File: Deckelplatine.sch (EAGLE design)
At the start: 67 parts, among them IC1 MAX1487EESA+, IC2 74HCT595D, IC3 74HCT595D, IC4 74HCT595D, IC5 74HCT595D, IC6 74HCT595D, J1 52808-2570, Q1 BC846BSMD, Q2 BC846BSMD, U1 LM2676S, X1 236-404, X2 233-502

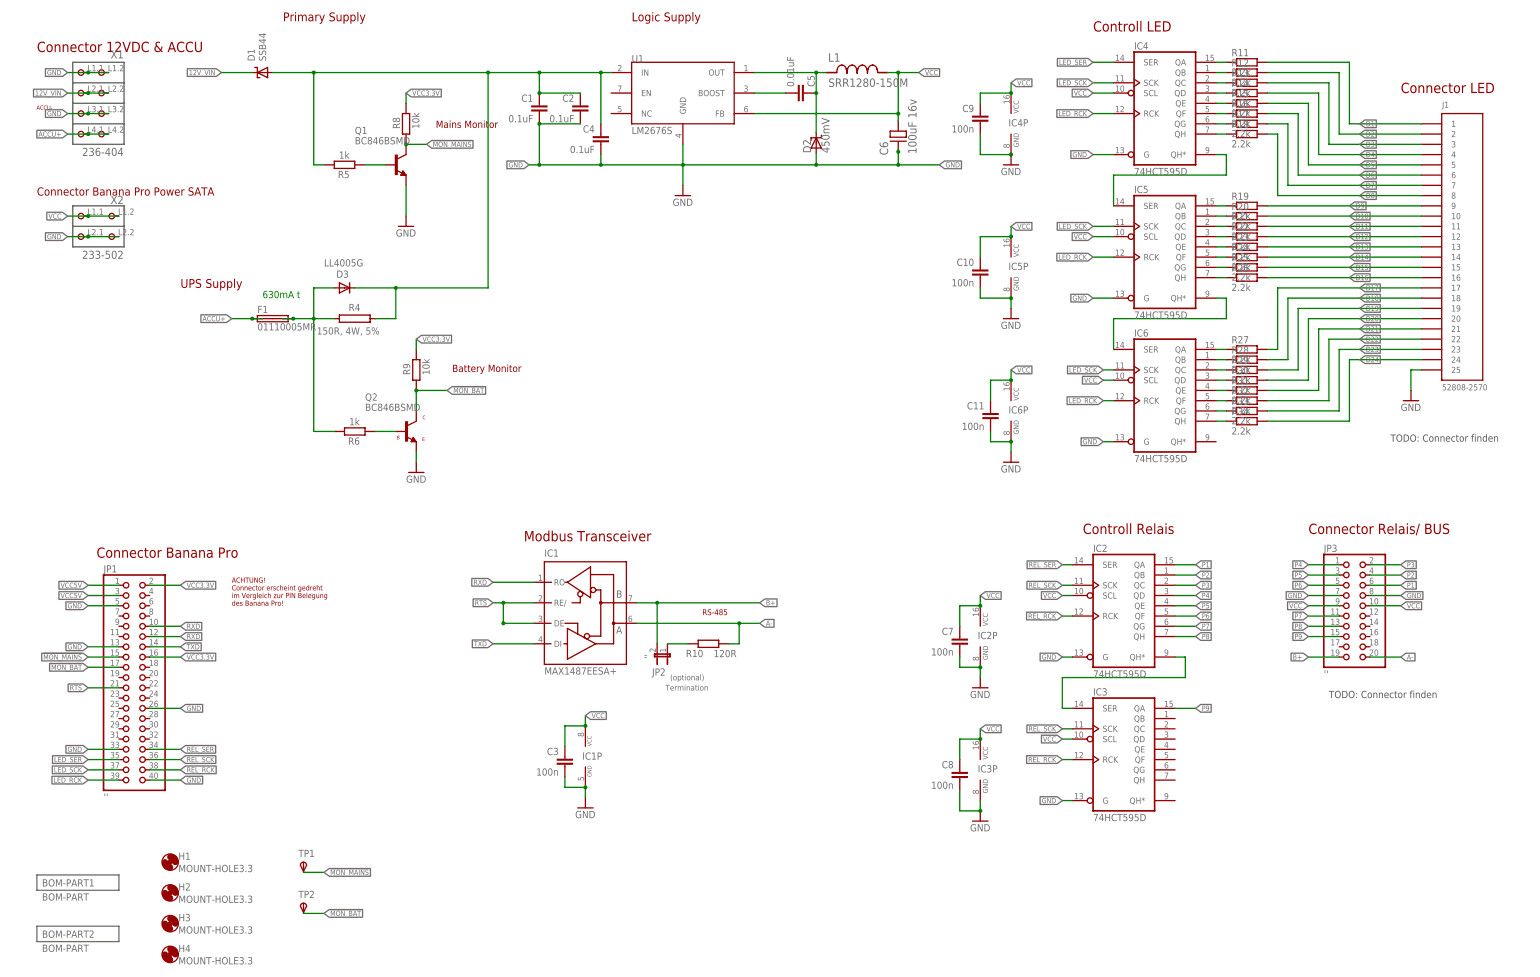
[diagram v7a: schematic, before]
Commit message: Schaltregler überarbeitet, Teil 1
CIN angepasst, Größe stimmte nicht (zu klein).
Materialliste Farnell an Schaltplan "webench_design_4385517_7_60043841.pdf" angepasst.
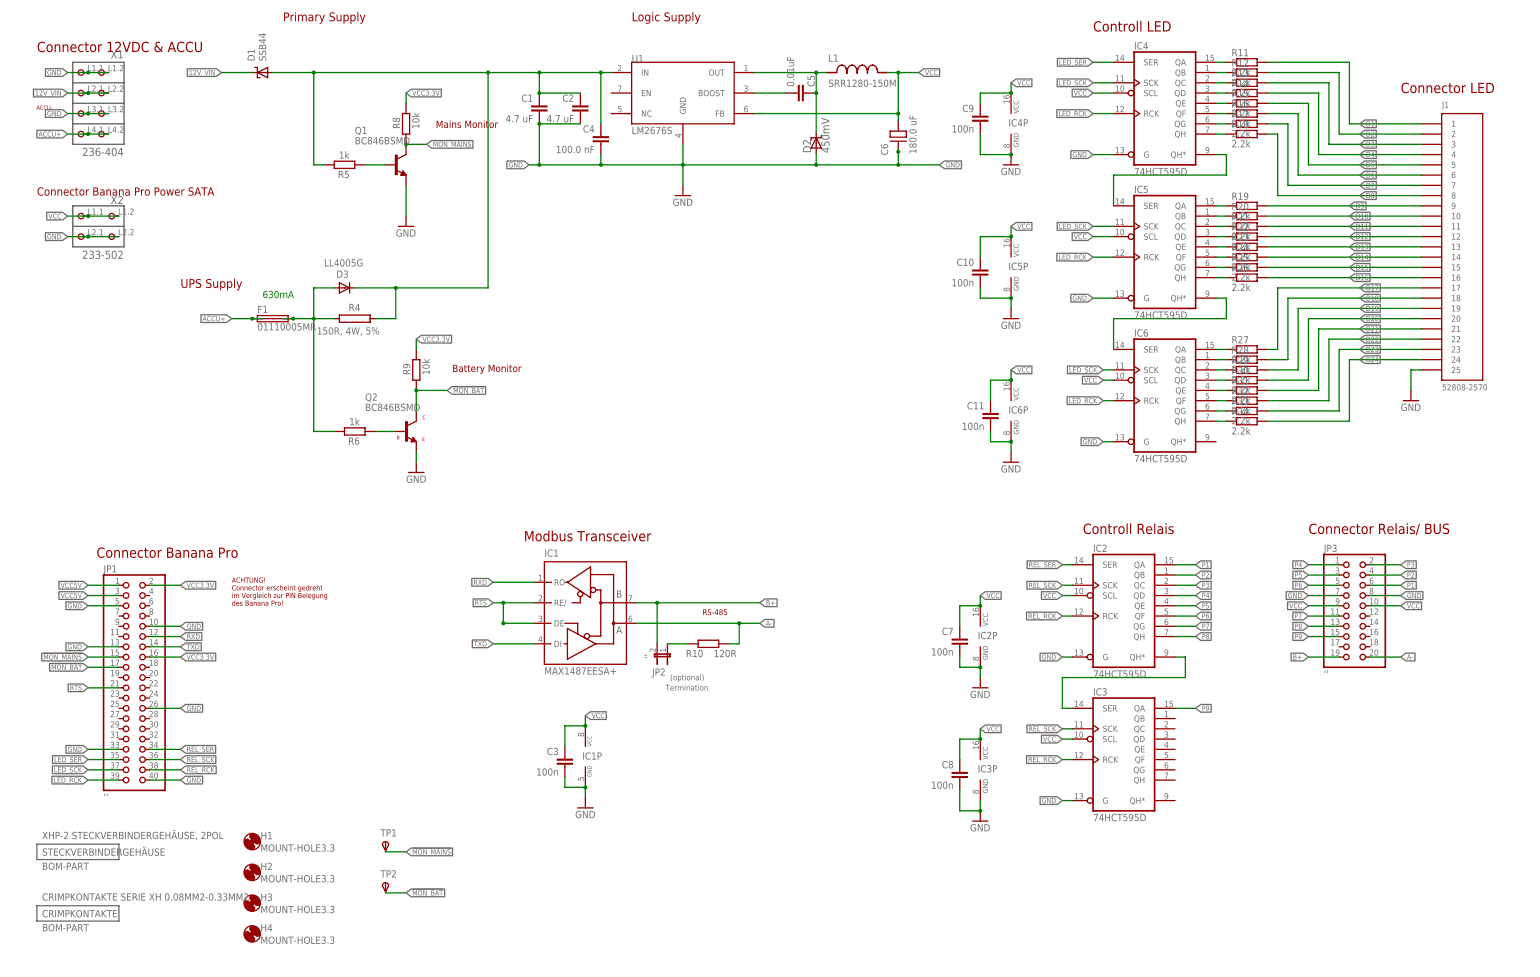
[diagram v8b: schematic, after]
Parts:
- C1, C2: value 0.1uF -> 4.7 uF; MF KEMET -> MURATA; MPN T495X475M050ATE300 -> GRM21BR61E475MA12L; OC_FARNELL 1692407 -> 2362111; PARTNO X7R-G1210 4,7 -> (none)
- C4: value 0.1uF -> 100.0 nF; MF KEMET -> AVX; MPN T495X475M050ATE300 -> 08053C104KAT2A; OC_FARNELL 1692407 -> 1740665; PARTNO X7R-G1210 4,7 -> (none)
- C5: MF AVX -> MURATA; MPN 0402YC103KAT2A -> GRM216R71H103KA01D; OC_FARNELL 1327662 -> 1828948; PARTNO X7R-G0805 10N -> (none)
- C6: value 100uF 16v -> 180.0 uF; device AcceleratedDesigns_Lib:16SVP180M -> AcceleratedDesigns_Lib:16SVP180MSM_RADIAL_10MM; MPN EEEFT1V561AP -> 16SVP180MX; OC_FARNELL 1868420 -> 2354685
- F1: MF (none) -> LITTELFUSE; MPN (none) -> 01110005MR
- H1, H2, H3, H4, TP1, TP2: OC_FARNELL (none) -> unknown
- L1: MF COILCRAFT -> BOURNS; MPN DO5022P-333MLD -> SRR1280-150M; OC_FARNELL 2287334 -> 2336471
- U1: MPN LM2676S-5.0/NOPB -> LM2676SX-5.0/NOPB; OC_FARNELL 1564684 -> 2435897; PARTNO LM 2676 S5,0 -> (none)
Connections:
- removed net N$1415: JP1.12
- net GND: now also JP1.10
- net RXD: now also JP1.12; no longer JP1.10
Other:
- note added: "630mA"
- note removed: "630mA t"
- note removed: "TODO: Connector finden"
- moved on the sheet: H1, H2, H3, H4, TP1, TP2
